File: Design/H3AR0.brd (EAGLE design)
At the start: 50.8 x 45.6 mm, 8 parts, among them P1 HEXABIT_17.60_REVERSED, U1 TPS76433DBVT

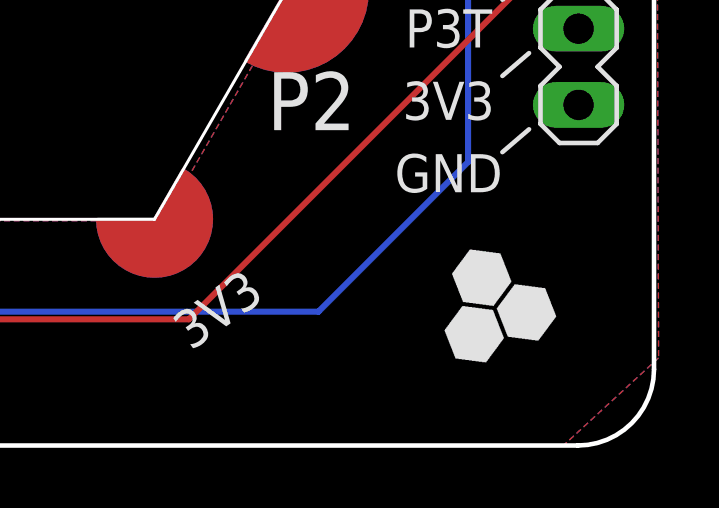
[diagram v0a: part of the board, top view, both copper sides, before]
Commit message: Update the logo
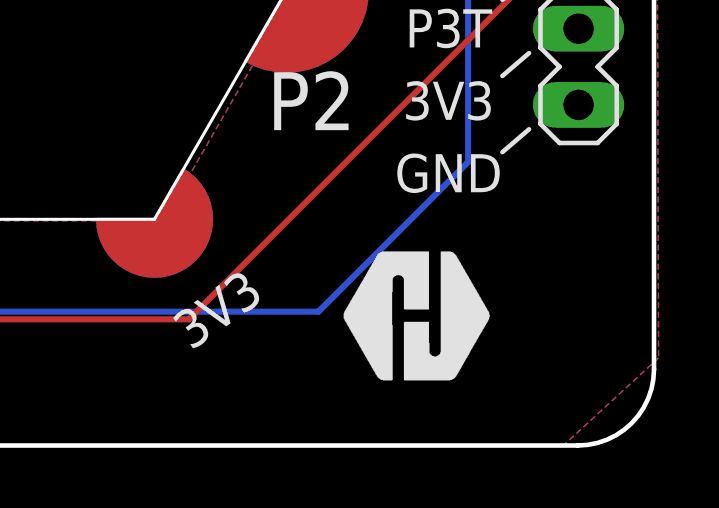
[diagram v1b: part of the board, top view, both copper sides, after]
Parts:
- added TRIMBLE-LOGO1: HEXA-LOGO, HEXABITZ_USER_INTERFACE_PARTS:HEXA-LOGO
